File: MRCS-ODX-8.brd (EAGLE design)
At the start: 97.8 x 68.6 mm, 15 parts

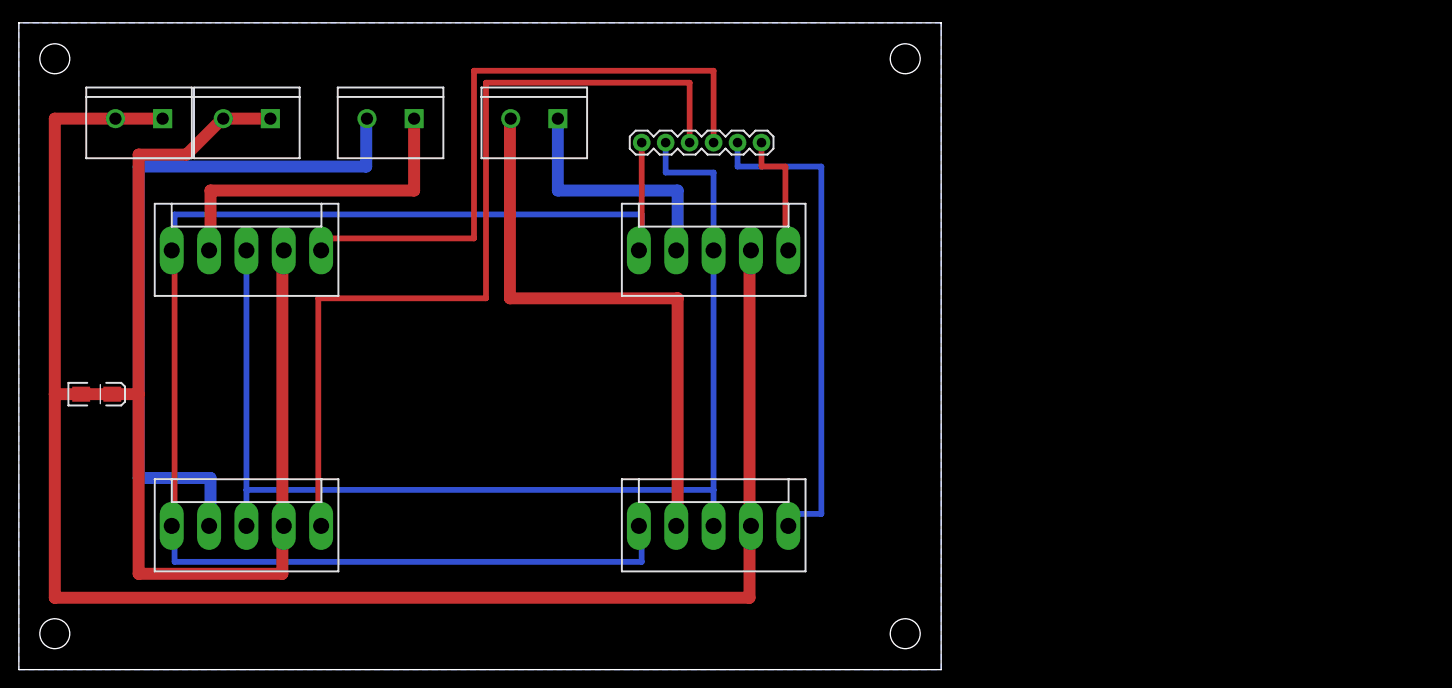
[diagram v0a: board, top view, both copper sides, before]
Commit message: Release Zero 20210405
prototypes.  Silkscreen on 3 position screw terminal has Track Common and GND reversed, needs adjustment of OD7 and expand needs to be moved inwards.  Otherwise electrically OK.  Track common bus on bottom can be cleaned up.
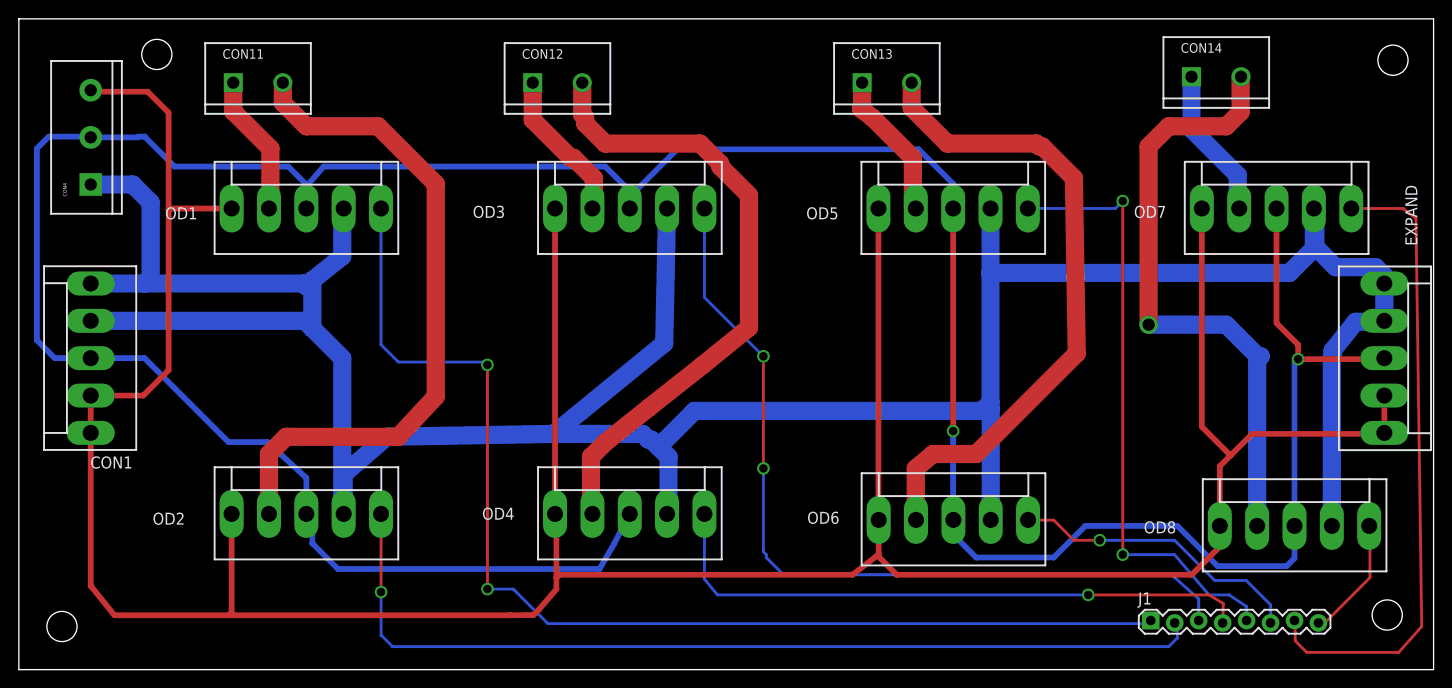
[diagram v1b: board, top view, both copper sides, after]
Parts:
- removed E$1, E$11, E$12, E$13: (no value), special-drill:DRILL_0.1250
- removed E$2: (no value), MRCSLogoTop:MRCSLOGOTOP
- removed E$3: (no value), SparkFun-Connectors.#1r:1X06
- removed E$5: SPLIT, SparkFun-Passives:EIA3216-KIT
- removed J2, J3: (no value), SparkFun:SCREWTERMINAL-5MM-2
- removed SECTA, SECTB: DCC IN, SparkFun:SCREWTERMINAL-5MM-2
- added CON1: INPUT (3.96), SPCoast:KK-156-5
- added CON11, CON12, CON13, CON14: (no value), SPCoast:SCREWTERMINAL-5MM-2
- added CON4: CONNECTOR-M035MM-LOCK, SPCoast:SCREWTERMINAL-5MM-3
- added EXPAND, OD5, OD6, OD7, OD8: (no value), SPCoast:KK-156-5
- added J1: (no value), SPCoast:1X08_LOCK
- added U$1: (no value), MRCSLogoTop:MRCSLOGOTOP
- added U$2: (no value), MRCSLogoBtm:MRCSLOGOBTM
- added U$3: (no value), MRCS-prop65warningBtm:CA-PROP65WARNING
- OD1, OD2, OD3, OD4: device con-molex:KK-156-5 -> SPCoast:KK-156-5
- moved OD1 43.4 mm to (30.5, 48.9)
- moved OD2 43.2 mm to (30.5, 16.5)
- moved OD3 40.9 mm to (64.8, 48.9)
- moved OD4 40.7 mm to (64.8, 16.5)
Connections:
- removed net S$21: SECTB.1
- removed net S$3: SECTA.1
- removed net S$4: J3.1
- removed net S$5: J2.1
- new net +12V: CON1.3, CON4.2, EXPAND.3, OD1.3, OD2.3, OD3.3, OD4.3, OD5.3, OD6.3, OD7.3, OD8.3
- new net GND: CON1.1, CON1.2, CON4.3, EXPAND.4, EXPAND.5, OD1.1, OD2.1, OD3.1, OD4.1, OD5.1, OD6.1, OD7.1, OD8.1
- new net N$1: CON14.2, OD8.2
- new net N$10: J1.2, OD2.5
- new net N$11: J1.1, OD1.5
- new net N$13: J1.4, OD4.5
- new net N$15: J1.5, OD5.5
- new net N$16: J1.6, OD6.5
- new net N$17: J1.8, OD8.5
- new net N$18: J1.7, OD7.5
- new net N$20: J1.3, OD3.5
- new net N$25: CON14.1, OD7.2
- new net N$26: CON12.2, OD4.2
- new net N$27: CON12.1, OD3.2
- new net N$28: CON11.2, OD2.2
- new net N$3: CON11.1, OD1.2
- new net N$5: CON13.2, OD6.2
- new net N$6: CON13.1, OD5.2
- new net TRACK_POWER: CON1.4, CON1.5, CON4.1, EXPAND.1, EXPAND.2, OD1.4, OD2.4, OD3.4, OD4.4, OD5.4, OD6.4, OD7.4, OD8.4
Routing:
- net GND: track 0.00 -> 345.2 mm
- net +12V: track 0.00 -> 338.2 mm, vias 0 -> 2
- net TRACK_POWER: track 0.00 -> 328.3 mm
- net S$3: track 144.1 -> 0.00 mm
- net N$11: track 0.00 -> 122.4 mm, vias 0 -> 2
- net S$10: track 102.9 -> 0.00 mm
- net N$10: track 0.00 -> 99.9 mm, vias 0 -> 1
- net S$6: track 92.1 -> 0.00 mm
- net N$20: track 0.00 -> 89.6 mm, vias 0 -> 2
- net S$21: track 84.1 -> 0.00 mm
- net S$2: track 73.7 -> 0.00 mm
- net N$28: track 0.00 -> 71.1 mm
- net N$5: track 0.00 -> 69.0 mm
- net S$8: track 67.9 -> 0.00 mm
- net N$18: track 0.00 -> 67.8 mm
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- removed copper zone on layer 16, net GND
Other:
- board size 97.8 x 68.6 mm -> 150 x 69 mm
- board text added: "8"
- board text added: "COM Vin GND"
- board text added: "Control Point Occupancy Detector Motherboard ODX-8 Seth Neumann 20210405"
- board text added: "Detection Output 1"
- board text added: "Expansion Pins 1. Track Com 2. Track Com 3. Vin 4. Logic Ground 5. Logic Ground"
- board text added: "ODX-8 cpOD Motherboard Seth Neumann 20210405"
- board text added: "Track 1 Track 2"
- board text added: "Track 3 Track 4"
- board text added: "Track 5 Track 6"
- board text added: "Track 7 Track 8"
- board text added: "cpOD Pins 1. Logic Ground 2. Track Out 3. Vin 4. Track Com 5. Detection Out"
- board text removed: "+Vin"
- board text removed: "0414-2015 v1.6"
- board text removed: "1"
- board text removed: "2"
- board text removed: "3"
- board text removed: "4"
- board text removed: "5"
- board text removed: "DCC"
- board text removed: "DCC In"
- board text removed: "GND"
- board text removed: "J1"
- board text removed: "Logic Gnd"
- board text removed: "MRCS Designs"
- board text removed: "OD1"
- board text removed: "OD2"
- board text removed: "OD3"
- board text removed: "OD4"
- board text removed: "ODX4 Occupancy Detector Extender"
- board text removed: "OccOut"
- board text removed: "OccOut 1"
- board text removed: "OccOut 2"
- board text removed: "OccOut 3"
- board text removed: "OccOut 4"
- board text removed: "Out"
- board text removed: "Sect A"
- board text removed: "Sect B"
- board text removed: "Top"
- board text removed: "Track Com"
- board text removed: "Track Out"
- board text removed: "cpNode ODX4"

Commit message: Rev 1.1
corrected Silk Screen error on input connector, moved OD7 connector to make more room.  Cleaned up track common bus.
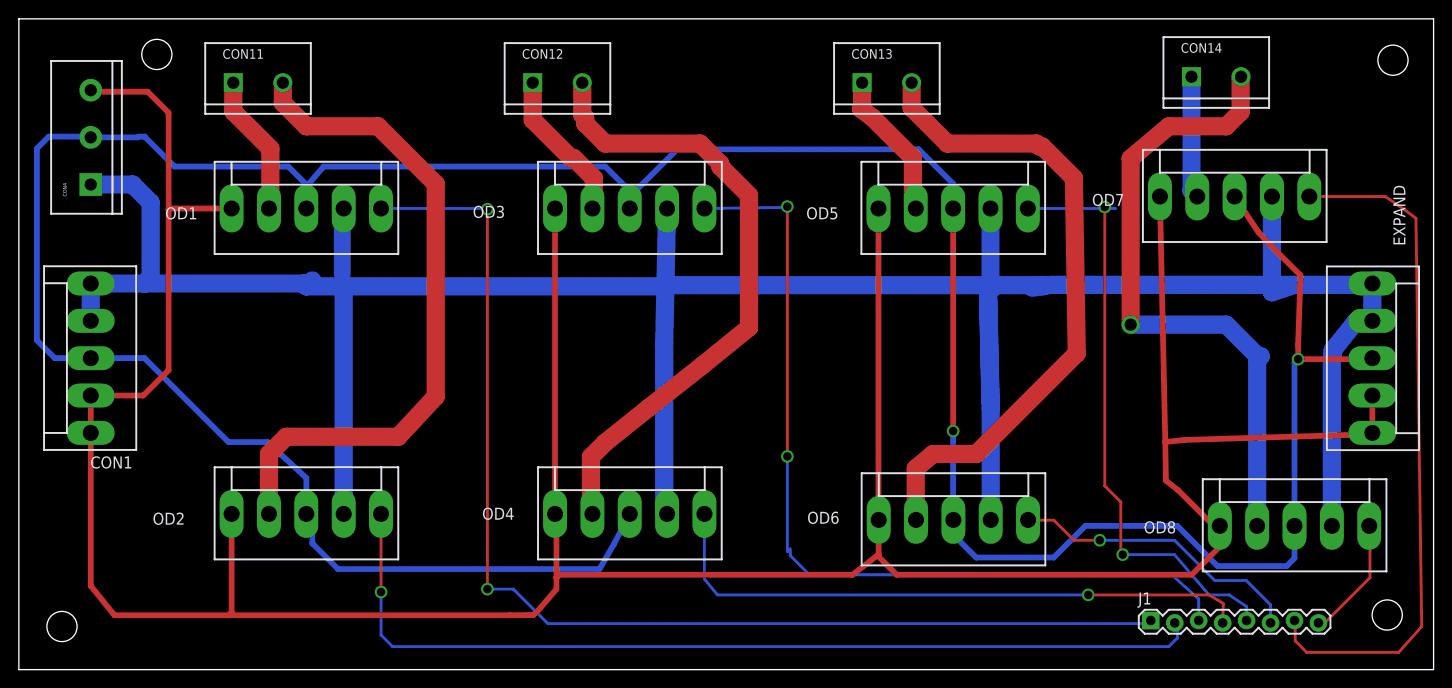
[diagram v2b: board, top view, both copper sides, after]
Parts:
- moved OD7 4.62 mm to (128.9, 50.2)
- moved EXPAND 1.27 mm to (143.5, 33.0)
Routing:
- net TRACK_POWER: track 328.3 -> 310.9 mm
- net GND: track 345.2 -> 354.8 mm
- net N$18: track 67.8 -> 72.7 mm
- net N$20: track 89.6 -> 93.8 mm
- net +12V: track 338.2 -> 342.1 mm
- net N$25: track 16.1 -> 13.0 mm
- net N$1: track 65.3 -> 68.2 mm
- net N$11: track 122.4 -> 123.6 mm
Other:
- board text added: "GND Vin COM"
- board text added: "ODX-8 cpOD Motherboard Seth Neumann 20210417"
- board text removed: "COM Vin GND"
- board text removed: "ODX-8 cpOD Motherboard Seth Neumann 20210405"

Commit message: minor changes and new gerbers
revised gerbers
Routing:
- net TRACK_POWER: track 310.9 -> 354.3 mm
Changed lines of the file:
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@@
 <setting verticaltext="up"/>
 </settings>
-<grid distance="25" unitdist="mil" unit="mil" style="dots" multiple="2" display="yes" altdistance="25" altunitdist="mil" altunit="mil"/>
+<grid distance="50" unitdist="mil" unit="mil" style="dots" multiple="2" display="yes" altdistance="25" altunitdist="mil" altunit="mil"/>
 <layers>
 <layer number="1" name="Top" color="4" fill="1" visible="yes" active="yes"/>
@@
 <wire x1="68.554090625" y1="40.640553125" x2="68.4252" y2="34.5924" width="1.9304" layer="16"/>
 <wire x1="103.02" y1="28.344" x2="102.743" y2="40.767" width="1.9304" layer="16"/>
-<wire x1="102.743" y1="40.767" x2="68.453" y2="40.767" width="1.9304" layer="16"/>
+<wire x1="102.743" y1="40.767" x2="73.66" y2="40.767" width="1.9304" layer="16"/>
+<wire x1="73.66" y1="40.767" x2="68.453" y2="40.767" width="1.9304" layer="16"/>
 <wire x1="103.0454" y1="15.875" x2="103.0454" y2="27.7138" width="1.9304" layer="16"/>
 <wire x1="103.0454" y1="27.7138" x2="102.761053125" y2="39.987765625" width="1.9304" layer="16"/>
@@
 <wire x1="68.4252" y1="34.5924" x2="68.4252" y2="16.8148" width="1.9304" layer="16"/>
 <wire x1="68.4252" y1="16.8148" x2="68.73" y2="16.51" width="1.9304" layer="16"/>
-<wire x1="109.37" y1="40.7924" x2="107.465" y2="40.49" width="1.9304" layer="16"/>
+<wire x1="109.37" y1="40.7924" x2="109.200090625" y2="40.765428125" width="1.9304" layer="16"/>
+<wire x1="109.200090625" y1="40.765428125" x2="107.465" y2="40.49" width="1.9304" layer="16"/>
 <wire x1="103.4132875" y1="40.64" x2="102.761053125" y2="39.987765625" width="1.9304" layer="16"/>
 <wire x1="103.02" y1="48.895" x2="103.02" y2="41.76" width="1.9304" layer="16"/>
@@
 <wire x1="132.865" y1="50.165" x2="132.865" y2="40.0074" width="1.9304" layer="16"/>
 <wire x1="132.865" y1="40.0074" x2="135.255" y2="40.7924" width="1.9304" layer="16"/>
-<wire x1="108.585" y1="40.64" x2="109.37" y2="40.7924" width="0" layer="19" extent="16-16"/>
+<wire x1="34.29" y1="41.91" x2="34.29" y2="40.64" width="0.4064" layer="16"/>
+<wire x1="103.02" y1="41.76" x2="108.20551875" y2="41.76" width="0.4064" layer="16"/>
+<wire x1="108.20551875" y1="41.76" x2="109.200090625" y2="40.765428125" width="0.4064" layer="16"/>
+<wire x1="109.200090625" y1="40.765428125" x2="73.661571875" y2="40.765428125" width="0.4064" layer="16"/>
+<wire x1="73.661571875" y1="40.765428125" x2="73.66" y2="40.767" width="0.4064" layer="16"/>
 <wire x1="68.554090625" y1="40.640553125" x2="68.453" y2="40.767" width="0" layer="19" extent="16-16"/>
 <wire x1="7.62" y1="40.64" x2="7.62" y2="40.94" width="0" layer="19" extent="16-16"/>
-<wire x1="103.02" y1="41.76" x2="102.743" y2="40.767" width="0" layer="19" extent="16-16"/>
-<wire x1="34.29" y1="41.91" x2="34.29" y2="40.64" width="0" layer="19" extent="16-16"/>
 </signal>
 <signal name="N$1">
